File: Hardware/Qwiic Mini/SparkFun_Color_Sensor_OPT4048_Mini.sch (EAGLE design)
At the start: 20 parts, among them J4 QWIIC_RIGHT_ANGLE, J5 QWIIC_RIGHT_ANGLE

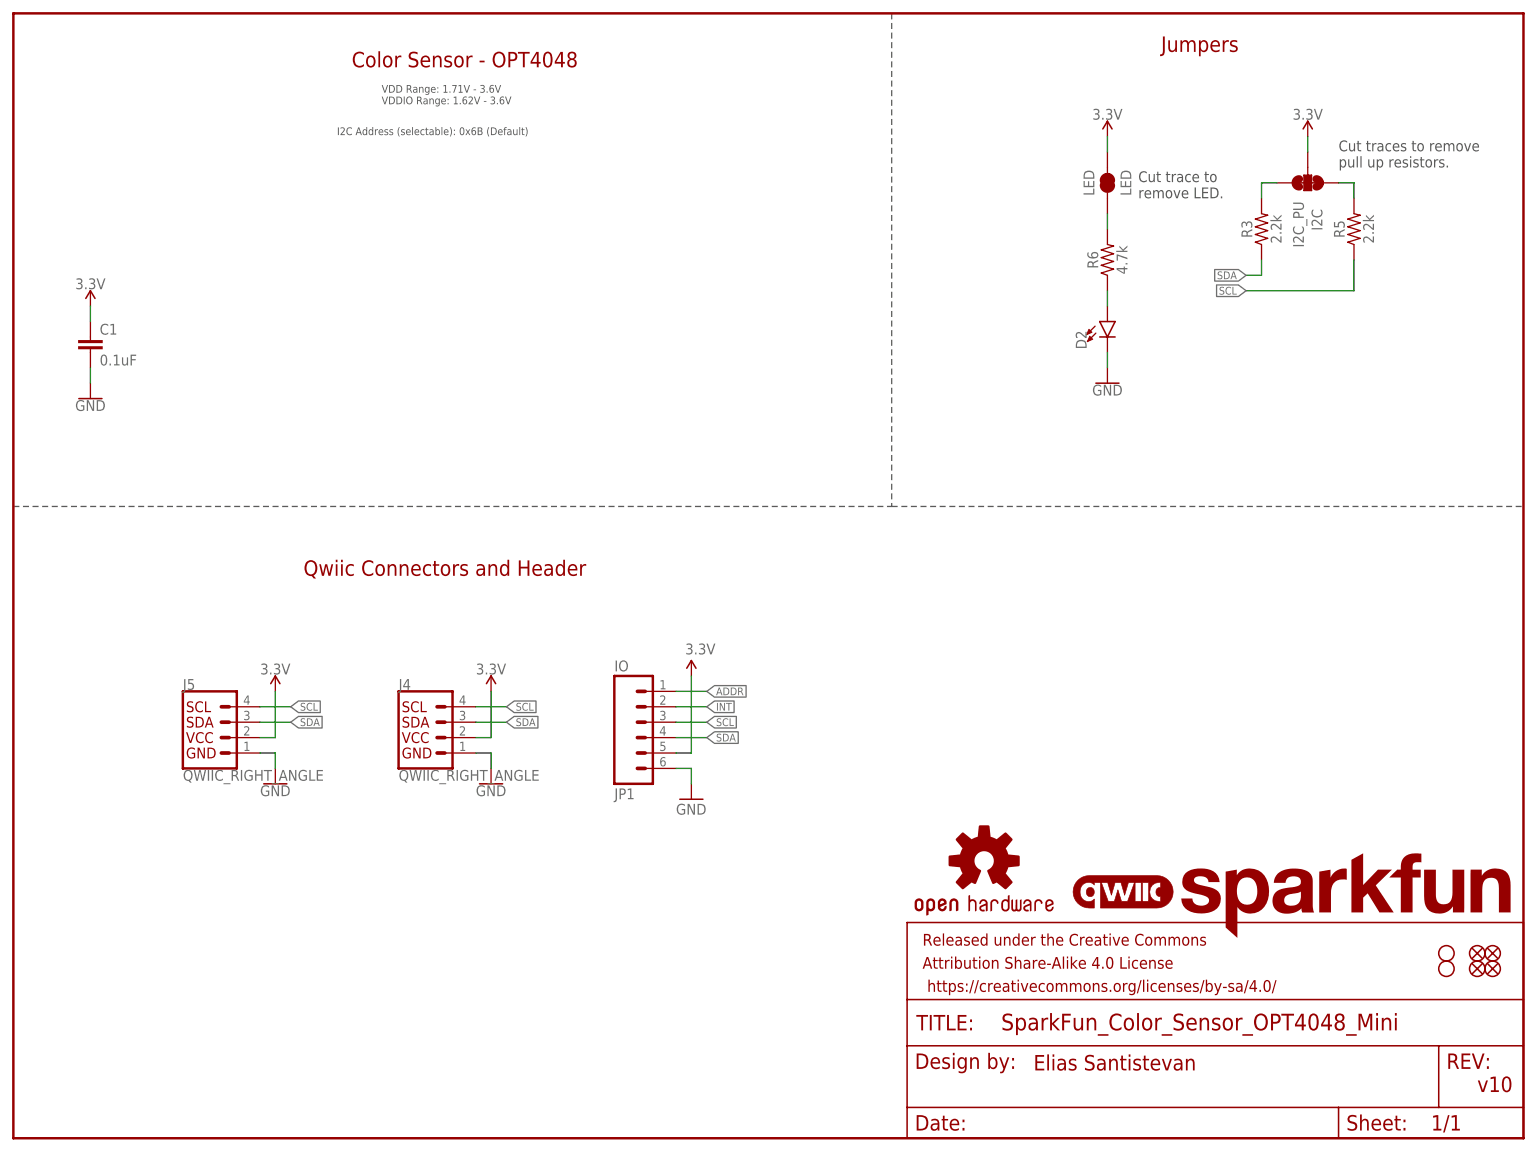
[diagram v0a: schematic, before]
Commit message: Finishes routing Qwiic mini
* Adds silk to Qwiic mini
* Adds ordering instructions
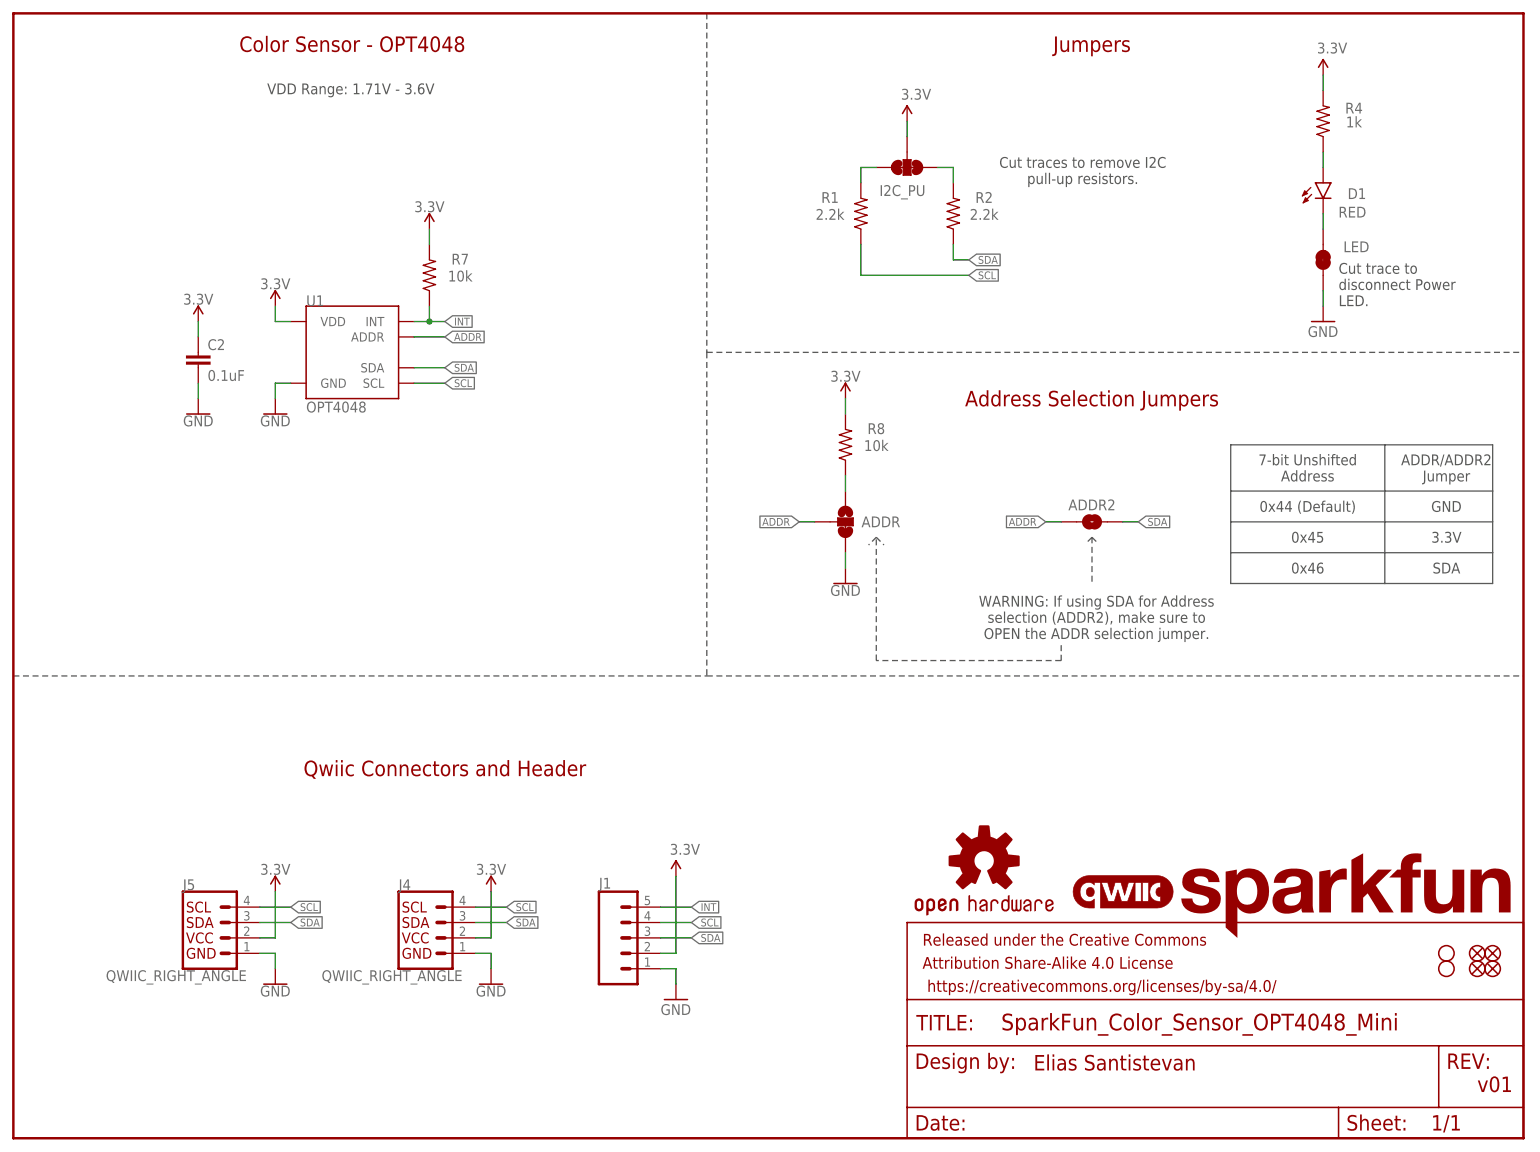
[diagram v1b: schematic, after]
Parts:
- removed C1: 0.1uF, SparkFun-Capacitors:0.1UF-0603-25V-(+80/-20%)
- removed D2: RED, SparkFun-LED:LED-RED_0603-KB
- removed I2C: I2C_PU, SparkFun-Jumpers:JUMPER-SMT_3_2-NC_TRACE_SILK
- removed JP1: IO, SparkFun-Connectors:CONN_06NO_SILK_NO_POP
- removed R3, R5: 2.2k, SparkFun-Resistors:2.2KOHM-0603-1/10W-1%
- removed R6: 4.7k, SparkFun-Resistors:4.7KOHM-0603-1/10W-1%
- added ADDR: JUMPER-SMT_3_1-NC_TRACE_SILK, SparkFun-Jumpers:JUMPER-SMT_3_1-NC_TRACE_SILK
- added ADDR2: JUMPER-SMT_2_NO_SILK, SparkFun-Jumpers:JUMPER-SMT_2_NO_SILK
- added C2: 0.1uF, SparkFun-Capacitors:0.1UF-0603-25V-(+80/-20%)
- added D1: RED, SparkFun-LED:LED-RED0603
- added I2C_PU: S_MODE, SparkFun-Jumpers:JUMPER-SMT_3_2-NC_TRACE_SILK
- added J1: (no value), SparkFun-Connectors:CONN_05NO_SILK
- added R1, R2: 2.2k, SparkFun-Resistors:2.2KOHM-0603-1/10W-1%
- added R4: 1k, SparkFun-Resistors:1KOHM-0603-1/10W-1%
- added R7, R8: 10k, SparkFun-Resistors:10KOHM-0603-1/10W-1%
- added U1: OPT4048, Color_Sensor:OPT4048
- LED: value LED -> JUMPER-SMT_2_NC_TRACE_SILK
- LOGO2: value QWIIC_LOGO_4MM -> QWIIC_LOGO_3MM; device SparkFun-Aesthetics:QWIIC_LOGO_4MM -> SparkFun-Aesthetics:QWIIC_LOGO_3MM
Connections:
- removed net N$5: D2.A, R6.1
- removed net N$6: LED.1, R6.2
- removed net N$7: I2C.3, R3.2
- removed net N$8: I2C.1, R5.2
- new net N$1: I2C_PU.1, R1.2
- new net N$2: I2C_PU.3, R2.2
- new net N$3: D1.A, R4.1
- new net N$4: D1.C, LED.2
- new net N$9: ADDR.1, R8.1
- net 3.3V: now also C2.1, I2C_PU.2, J1.2, R4.2, R7.2, R8.2, U1.VDD; no longer C1.1, I2C.2, JP1.5, LED.2
- net ADDR: now also ADDR.2, ADDR2.1, U1.ADDR; no longer JP1.1
- net GND: now also ADDR.3, C2.2, J1.1, LED.1, U1.GND; no longer C1.2, D2.C, JP1.6
- net INT: now also J1.5, R7.1, U1.INT; no longer JP1.2
- net SCL: now also J1.4, R1.1, U1.SCL; no longer JP1.3, R5.1
- net SDA: now also ADDR2.2, J1.3, R2.1, U1.SDA; no longer JP1.4, R3.1
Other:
- note added: "0x44 (Default)"
- note added: "0x45"
- note added: "0x46"
- note added: "3.3V"
- note added: "7-bit Unshifted Address"
- note added: "ADDR/ADDR2 Jumper"
- note added: "Address Selection Jumpers"
- note added: "Cut trace to disconnect Power LED."
- note added: "Cut traces to remove I2C pull-up resistors."
- note added: "GND"
- note added: "SDA"
- note added: "VDD Range: 1.71V - 3.6V"
- note added: "WARNING: If using SDA for Address selection (ADDR2), make sure to OPEN the ADDR selection jumper."
- note added: "v01"
- note removed: "Cut trace to remove LED."
- note removed: "Cut traces to remove pull up resistors."
- note removed: "I2C Address (selectable): 0x6B (Default)"
- note removed: "VDD Range: 1.71V - 3.6V VDDIO Range: 1.62V - 3.6V"
- note removed: "v10"
- moved on the sheet: J4, J5, LED

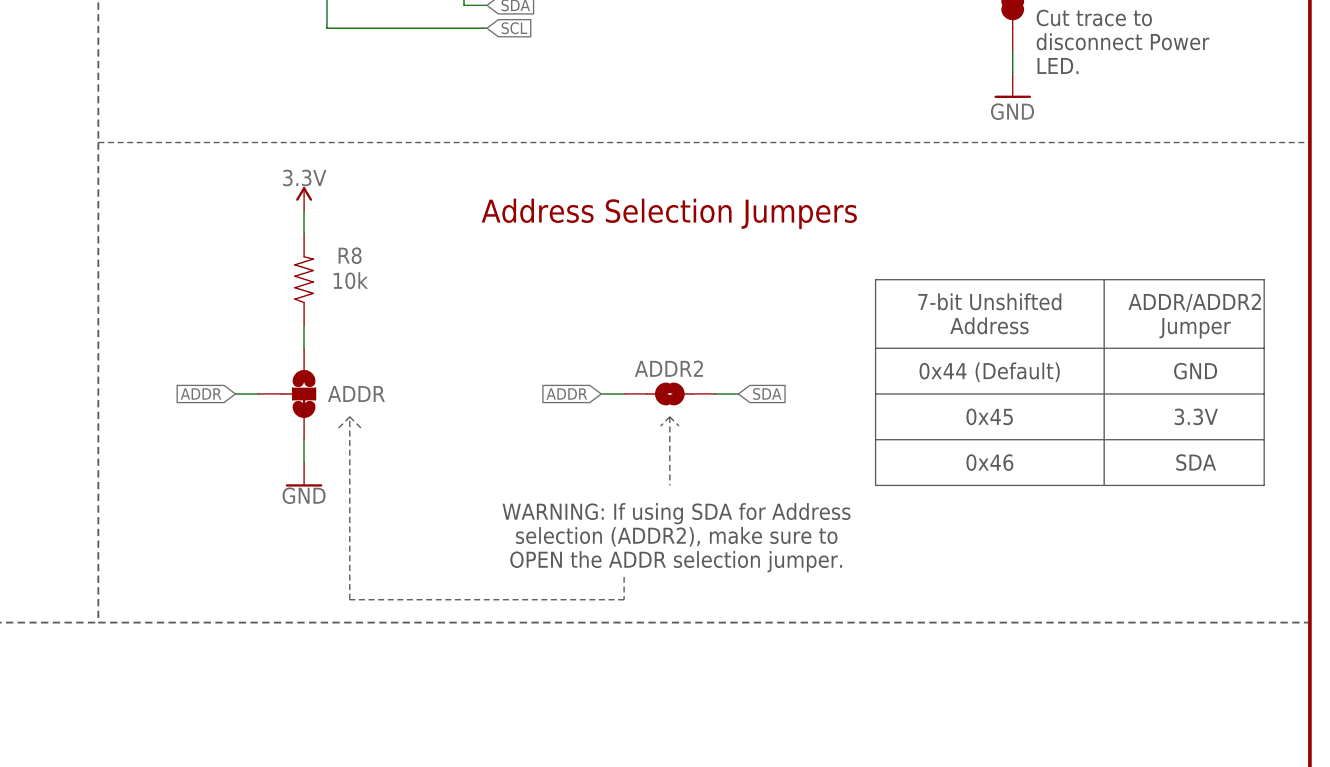
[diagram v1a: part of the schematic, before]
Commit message: Changes address selection on the mini
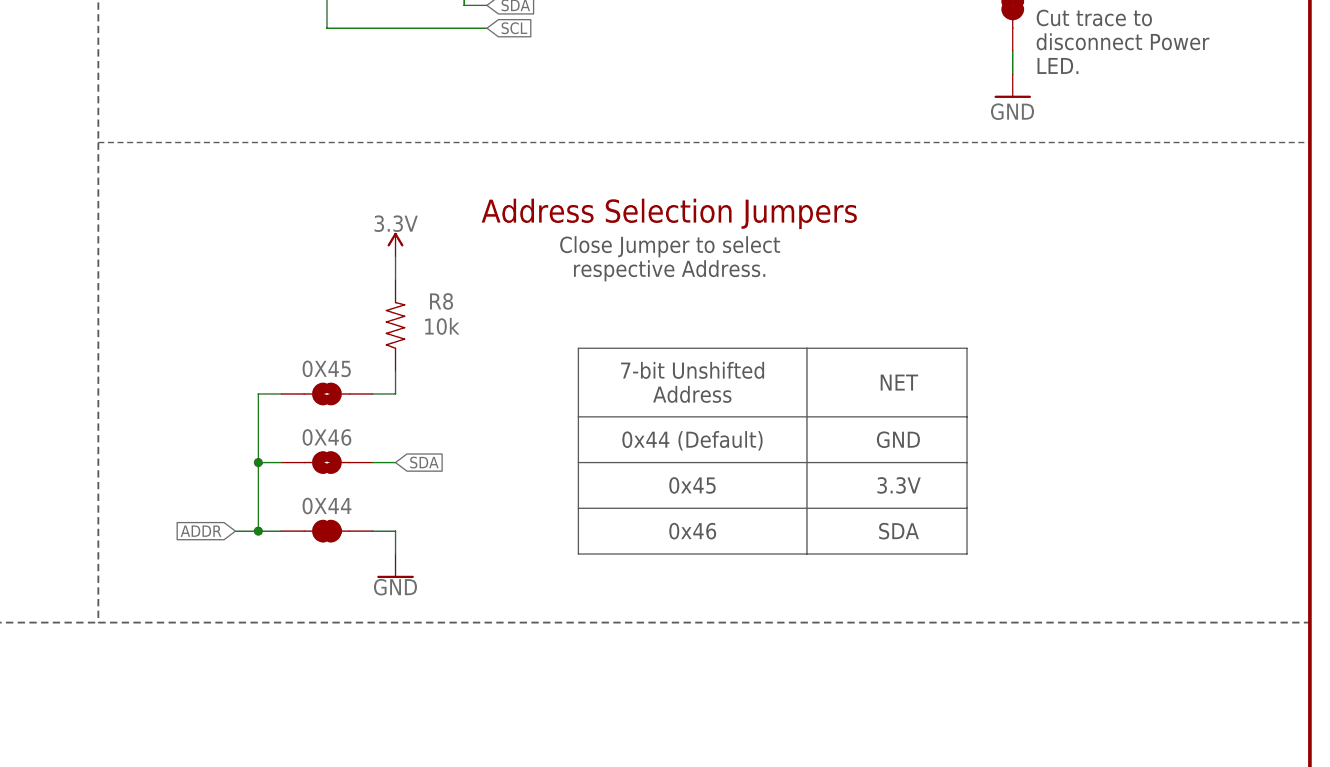
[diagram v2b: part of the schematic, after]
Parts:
- removed ADDR: JUMPER-SMT_3_1-NC_TRACE_SILK, SparkFun-Jumpers:JUMPER-SMT_3_1-NC_TRACE_SILK
- removed ADDR2: JUMPER-SMT_2_NO_SILK, SparkFun-Jumpers:JUMPER-SMT_2_NO_SILK
- added 0X44: JUMPER-SMT_2_NC_TRACE_SILK, SparkFun-Jumpers:JUMPER-SMT_2_NC_TRACE_SILK
- added 0X45, 0X46: JUMPER-SMT_2_NO_SILK, SparkFun-Jumpers:JUMPER-SMT_2_NO_SILK
- C2: device SparkFun-Capacitors:0.1UF-0603-25V-(+80/-20%) -> SparkFun-Capacitors:0.1UF-0402T-16V-10%
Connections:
- net ADDR: now also 0X44.1, 0X45.1, 0X46.1; no longer ADDR.2, ADDR2.1
- net GND: now also 0X44.2; no longer ADDR.3
- net N$9: now also 0X45.2; no longer ADDR.1
- net SDA: now also 0X46.2; no longer ADDR2.2
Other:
- note added: "Close Jumper to select respective Address."
- note added: "NET"
- note removed: "ADDR/ADDR2 Jumper"
- note removed: "WARNING: If using SDA for Address selection (ADDR2), make sure to OPEN the ADDR selection jumper."
- moved on the sheet: R8

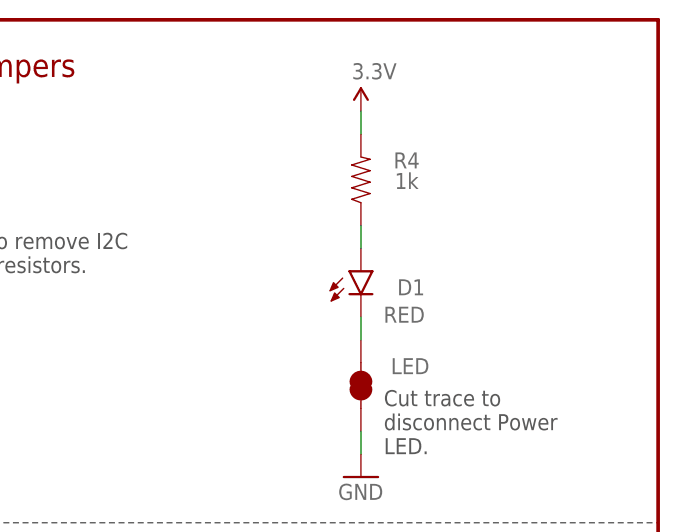
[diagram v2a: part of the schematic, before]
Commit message: Adds correct red LEDs and their resistors, updates PROD_ID for part.
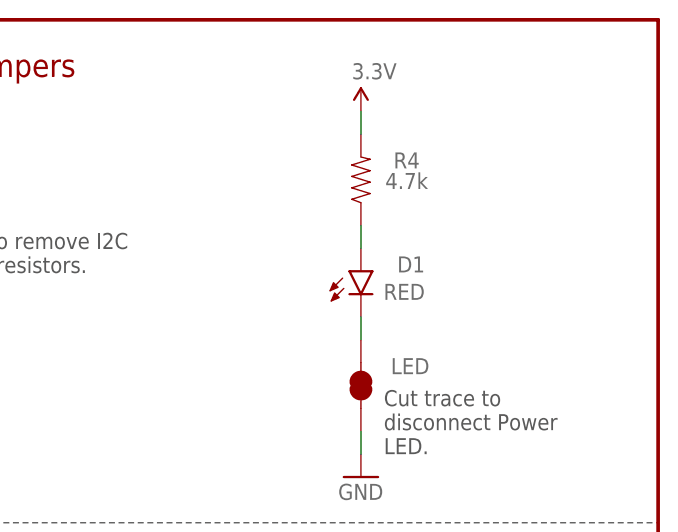
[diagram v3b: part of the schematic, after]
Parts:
- D1: device SparkFun-LED:LED-RED0603 -> SparkFun-LED:LED-RED_0603-KB
- R4: value 1k -> 4.7k; device SparkFun-Resistors:1KOHM-0603-1/10W-1% -> SparkFun-Resistors:4.7KOHM-0603-1/10W-1%
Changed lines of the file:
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@@
 <part name="SUPPLY4" library="SparkFun-PowerSymbols" deviceset="3.3V" device=""/>
 <part name="I2C_PU" library="SparkFun-Jumpers" deviceset="JUMPER-SMT_3_2-NC_TRACE" device="_SILK" package3d_urn="urn:adsk.eagle:package:39289/1" value="S_MODE"/>
-<part name="D1" library="SparkFun-LED" deviceset="LED-RED" device="0603" value="RED"/>
-<part name="R4" library="SparkFun-Resistors" deviceset="1KOHM" device="-0603-1/10W-1%" value="1k"/>
+<part name="D1" library="SparkFun-LED" deviceset="LED-RED" device="_0603-KB" value="RED"/>
+<part name="R4" library="SparkFun-Resistors" deviceset="4.7KOHM" device="-0603-1/10W-1%" value="4.7k"/>
 <part name="LED" library="SparkFun-Jumpers" deviceset="JUMPER-SMT_2_NC_TRACE" device="_SILK" package3d_urn="urn:adsk.eagle:package:39281/1"/>
 <part name="SUPPLY5" library="SparkFun-PowerSymbols" deviceset="3.3V" device=""/>
@@
 </instance>
 <instance part="D1" gate="G$1" x="215.9" y="157.48" smashed="yes">
-<attribute name="NAME" x="223.012" y="156.591" size="1.778" layer="95" font="vector" rot="R180"/>
-<attribute name="VALUE" x="223.012" y="151.765" size="1.778" layer="96" font="vector" rot="R180" align="top-left"/>
+<attribute name="NAME" x="223.012" y="159.131" size="1.778" layer="95" font="vector" rot="R180"/>
+<attribute name="VALUE" x="223.012" y="154.305" size="1.778" layer="96" font="vector" rot="R180" align="top-left"/>
 </instance>
 <instance part="R4" gate="G$1" x="215.9" y="167.64" smashed="yes" rot="R90">
@@
 <segment>
 <pinref part="U1" gate="G$1" pin="SCL"/>
-<wire x1="71.12" y1="124.46" x2="66.04" y2="124.46" width="0.127" layer="91"/>
+<wire x1="71.12" y1="124.46" x2="66.04" y2="124.46" width="0.1524" layer="91"/>
 <label x="71.12" y="124.46" size="1.27" layer="95" font="vector" xref="yes"/>
 </segment>
@@
 <segment>
 <pinref part="U1" gate="G$1" pin="SDA"/>
-<wire x1="71.12" y1="127" x2="66.04" y2="127" width="0.127" layer="91"/>
+<wire x1="71.12" y1="127" x2="66.04" y2="127" width="0.1524" layer="91"/>
 <label x="71.12" y="127" size="1.27" layer="95" font="vector" xref="yes"/>
 </segment>
